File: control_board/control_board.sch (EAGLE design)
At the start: 37 parts, among them IC1 ATMEGA1284P-MU, J1 USB Female Type C Connector, Q1 220mA/50V/3.5Ω, SW1 SPST_TACT-KMR2, U1 915MHz, U3 MCP73833

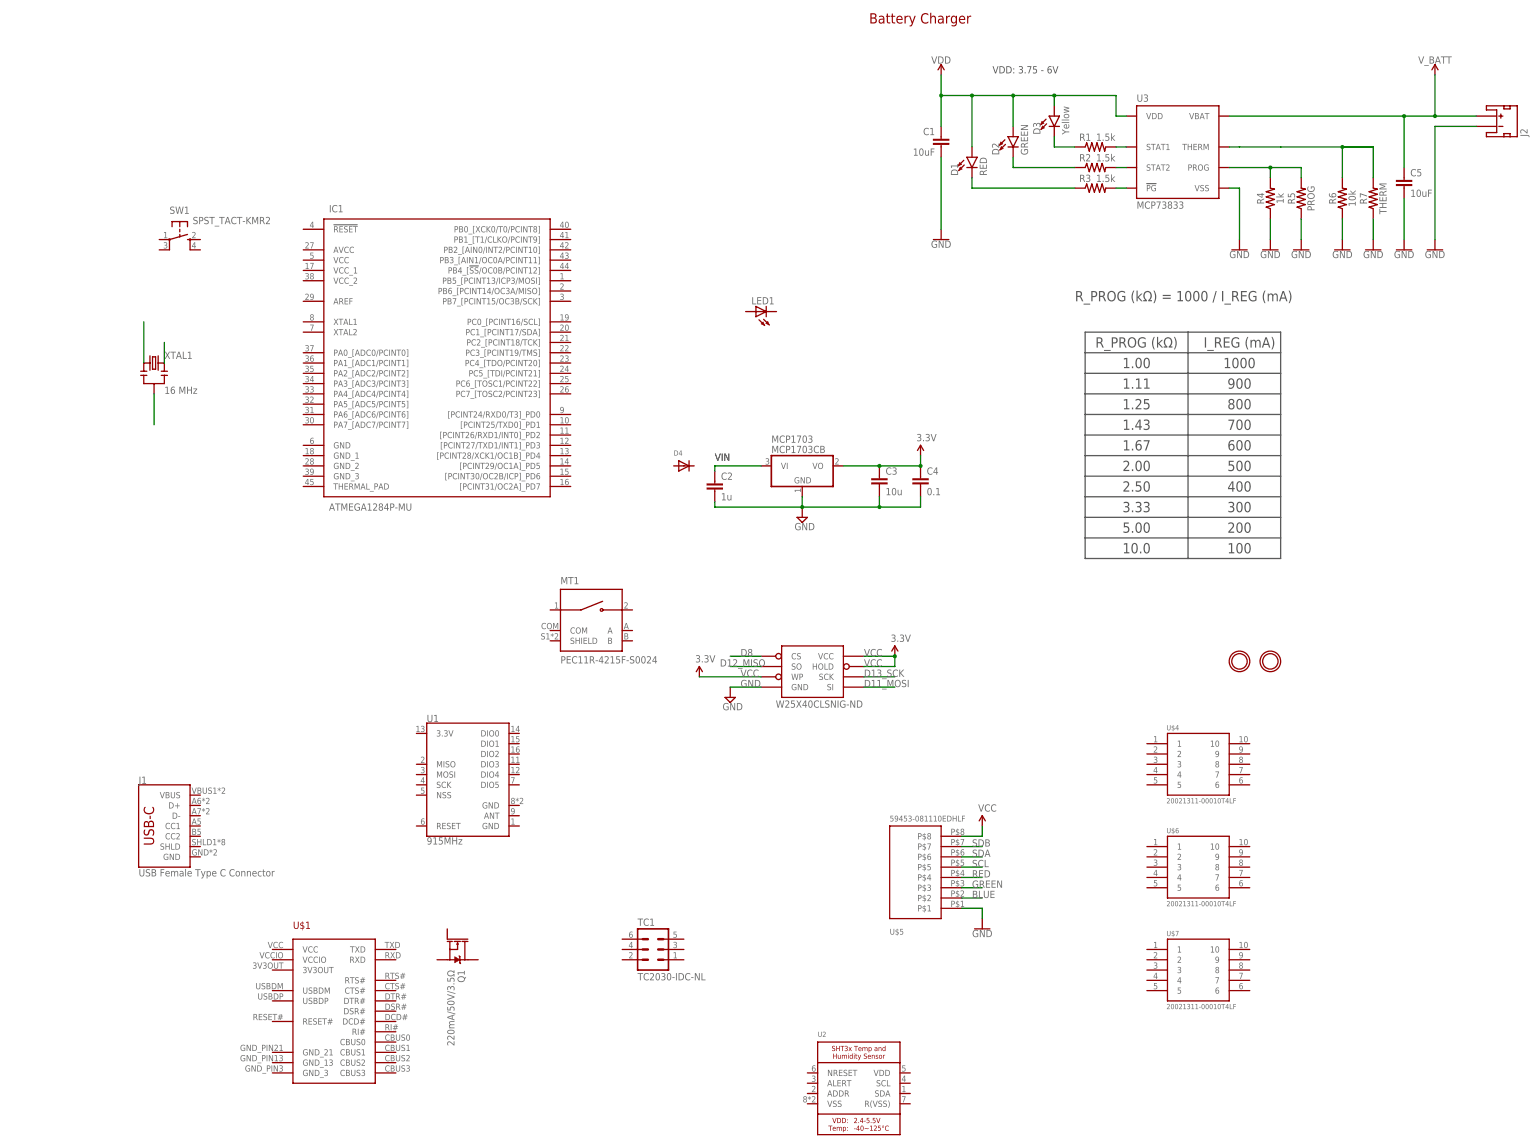
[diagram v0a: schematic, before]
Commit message: updated control board (unfinished)
- Schematic complete
- all components placed on board in roughly the approx. location
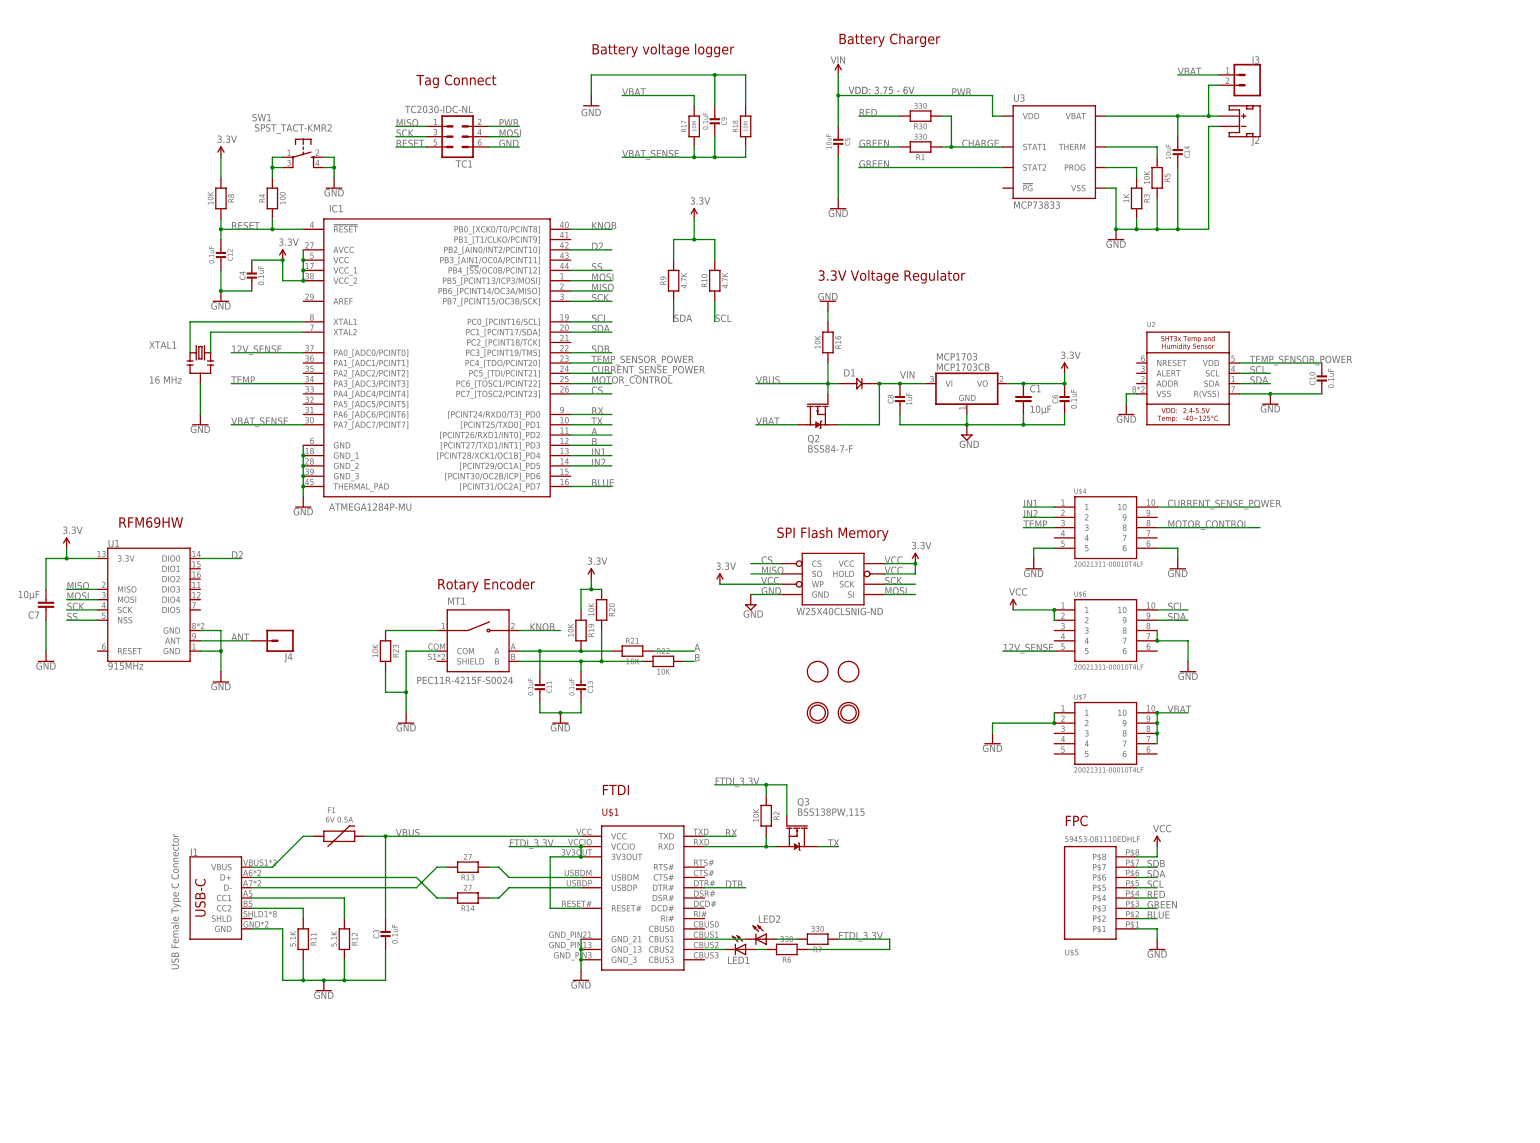
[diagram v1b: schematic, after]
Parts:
- removed C2: 1u, LowPowerLab:CAP0603-CAP
- removed D2: GREEN, SparkFun-LED:LED-GREEN0603
- removed D3: Yellow, SparkFun-LED:LED-YELLOW0603
- removed D4: (no value), adafruit:DIODESOD-123
- removed Q1: 220mA/50V/3.5Ω, SparkFun-DiscreteSemi:MOSFET-NCH-BSS138
- added C10, C11, C12, C13, C6, C9: 0.1uF, Adafruit Feather 32u4 Bluefruit LE:MICROBUILDER_CAP_CERAMIC_0402MP
- added C14: 10uF, Adafruit Feather 32u4 Bluefruit LE:MICROBUILDER_CAP_CERAMIC_0402MP
- added C7: 10µF, SparkFun-Capacitors:0.33UF/330NF-0805-50V-10%
- added C8: 1uF, Adafruit Feather 32u4 Bluefruit LE:MICROBUILDER_CAP_CERAMIC_0402MP
- added F1: 6V 0.5A, SparkFun-Fuses:PPTC_6V500MA
- added J3: (no value), SparkFun-Connectors:CONN_02
- added J4: (no value), SparkFun-Connectors:CONN_01
- added LED2: (no value), adafruit:LEDCHIPLED_0603
- added Q2: BSS84-7-F, MOSFETs:MOSFET-PCH-BSS84
- added Q3: BSS138PW,115, MOSFETs:MOSFET-NCH-BSS138PW,115
- added R10, R9: 4.7K, Adafruit Feather 32u4 Bluefruit LE:MICROBUILDER_RESISTOR_0402MP
- added R11, R12: 5.1K, Adafruit Feather 32u4 Bluefruit LE:MICROBUILDER_RESISTOR_0402MP
- added R13, R14: 27, Adafruit Feather 32u4 Bluefruit LE:MICROBUILDER_RESISTOR_0402MP
- added R16, R19, R20, R21, R22, R23, R8: 10K, Adafruit Feather 32u4 Bluefruit LE:MICROBUILDER_RESISTOR_0402MP
- added R17, R18: 10M, Adafruit Feather 32u4 Bluefruit LE:MICROBUILDER_RESISTOR_0402MP
- added R30: 330, Adafruit Feather 32u4 Bluefruit LE:MICROBUILDER_RESISTOR_0402MP
- added U$8, U$9: FIDUCIAL, adafruit:FIDUCIAL
- C1: value 10uF -> 10µF; device SparkFun-Capacitors:10UF-0603-6.3V-20% -> SparkFun-Capacitors:0.33UF/330NF-0805-50V-10%
- C3: value 10u -> 0.1uF; device LowPowerLab:CAP0805-CAP -> Adafruit Feather 32u4 Bluefruit LE:MICROBUILDER_CAP_CERAMIC_0402MP; MPN (none) -> GRM155R71C104KA88J
- C4: value 0.1 -> 0.1uF; device LowPowerLab:CAP0603-CAP -> Adafruit Feather 32u4 Bluefruit LE:MICROBUILDER_CAP_CERAMIC_0402MP; MPN (none) -> GRM155R71C104KA88J
- C5: device SparkFun-Capacitors:10UF-0603-6.3V-20% -> Adafruit Feather 32u4 Bluefruit LE:MICROBUILDER_CAP_CERAMIC_0402MP; MPN (none) -> GRM155R71C104KA88J
- D1: value RED -> (none); device SparkFun-LED:LED-RED0603 -> SCHOTTKY_0805:DIODE_SCHOTTKY0805-RES
- LED1: device adafruit:LEDCHIPLED_0805 -> adafruit:LEDCHIPLED_0603
- R1: value 1.5k -> 330; device SparkFun-Resistors:1.5KOHM-0603-1/10W-1% -> Adafruit Feather 32u4 Bluefruit LE:MICROBUILDER_RESISTOR_0402MP; MPN (none) -> RC0402FR-7W10KL
- R2: value 1.5k -> 10K; device SparkFun-Resistors:1.5KOHM-0603-1/10W-1% -> Adafruit Feather 32u4 Bluefruit LE:MICROBUILDER_RESISTOR_0402MP; MPN (none) -> RC0402FR-7W10KL
- R3: value 1.5k -> 1K; device SparkFun-Resistors:1.5KOHM-0603-1/10W-1% -> Adafruit Feather 32u4 Bluefruit LE:MICROBUILDER_RESISTOR_0402MP; MPN (none) -> RC0402FR-7W10KL
- R4: value 1k -> 100; device SparkFun-Resistors:1KOHM-0603-1/10W-1% -> Adafruit Feather 32u4 Bluefruit LE:MICROBUILDER_RESISTOR_0402MP; MPN (none) -> RC0402FR-7W10KL
- R5: value PROG -> 10K; device SparkFun-Resistors:RESISTORAXIAL-0.3 -> Adafruit Feather 32u4 Bluefruit LE:MICROBUILDER_RESISTOR_0402MP; MPN (none) -> RC0402FR-7W10KL
- R6: value 10k -> 330; device SparkFun-Resistors:10KOHM-0603-1/10W-1% -> Adafruit Feather 32u4 Bluefruit LE:MICROBUILDER_RESISTOR_0402MP; MPN (none) -> RC0402FR-7W10KL
- R7: value THERM -> 330; device SparkFun-Resistors:RESISTORAXIAL-0.3 -> Adafruit Feather 32u4 Bluefruit LE:MICROBUILDER_RESISTOR_0402MP; MPN (none) -> RC0402FR-7W10KL
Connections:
- removed net D11_MOSI: W25X40CLSNIG-ND.SI
- removed net D12_MISO: W25X40CLSNIG-ND.SO
- removed net D13_SCK: W25X40CLSNIG-ND.SCK
- removed net D8: W25X40CLSNIG-ND.CS
- removed net GND1: XTAL1.2
- removed net N$21: XTAL1.3
- removed net PG: R3.2, U3.!PG
- removed net STAT1: R1.2, U3.STAT1
- removed net STAT2: R2.2, U3.STAT2
- removed net VDD: C1.1, D1.A, D2.A, D3.A, U3.VDD
- removed net V_BATT: C5.1, J2.+, U3.VBAT
- new net 12V_SENSE: IC1.PA0_[ADC0/PCINT0], U$6.5
- new net A: C11.2, IC1.[PCINT26/RXD1/INT0]_PD2, MT1.A, R19.2, R21.1, R21.2
- new net ANT: J4.1, U1.ANT
- new net B: C13.2, IC1.[PCINT27/TXD1/INT1]_PD3, MT1.B, R20.2, R22.1, R22.2
- new net CHARGE: R1.1, R30.1, U3.STAT1
- new net CS: IC1.PC7_[TOSC2/PCINT23], W25X40CLSNIG-ND.CS
- new net CURRENT_SENSE_POWER: IC1.PC5_[TDI/PCINT21], U$4.10
- new net D2: IC1.PB2_[AIN0/INT2/PCINT10], U1.DIO0
- new net DTR: U$1.DTR#
- new net FTDI_3.3V: Q3.G, R2.1, R6.1, R7.1, U$1.3V3OUT, U$1.RESET#, U$1.VCCIO
- new net IN1: IC1.[PCINT28/XCK1/OC1B]_PD4, U$4.1
- new net IN2: IC1.[PCINT29/OC1A]_PD5, U$4.2
- new net KNOB: IC1.PB0_[XCK0/T0/PCINT8], MT1.2
- new net MISO: IC1.PB6_[PCINT14/OC3A/MISO], TC1.1, U1.MISO, W25X40CLSNIG-ND.SO
- new net MOSI: IC1.PB5_[PCINT13/ICP3/MOSI], TC1.4, U1.MOSI, W25X40CLSNIG-ND.SI
- new net MOTOR_CONTROL: IC1.PC6_[TOSC1/PCINT22], U$4.8
- new net N$10: F1.1, J1.VBUS
- new net N$11: MT1.1, R23.1
- new net N$12: R4.2, SW1.P, SW1.P1
- new net N$13: LED1.C, U$1.CBUS2
- new net N$14: Q3.S, R2.2, U$1.RXD
- new net N$15: LED1.A, R6.2
- new net N$17: LED2.A, R7.2
- new net N$18: LED2.C, U$1.CBUS1
- new net N$2: C14.2, J2.+, J3.2, U3.VBAT
- new net N$3: IC1.XTAL2, XTAL1.3
- new net N$7: J1.D-, R13.2
- new net N$8: R14.1, U$1.USBDP
- new net N$9: R13.1, U$1.USBDM
- new net PWR: C5.2, TC1.2, U3.VDD
- new net RESET: C12.2, IC1.!RESET, R4.1, R8.2, TC1.5
- new net RX: IC1.[PCINT24/RXD0/T3]_PD0, U$1.TXD
- new net SCK: IC1.PB7_[PCINT15/OC3B/SCK], TC1.3, U1.SCK, W25X40CLSNIG-ND.SCK
- new net SS: IC1.PB4_[!SS!/OC0B/PCINT12], U1.NSS
- new net TEMP: IC1.PA3_[ADC3/PCINT3], U$4.3
- new net TEMP_SENSOR_POWER: C10.1, IC1.PC4_[TDO/PCINT20], U2.VDD
- new net TX: IC1.[PCINT25/TXD0]_PD1, Q3.D
- new net VBAT: J3.1, Q2.D1, R17.2, U$7.10, U$7.7, U$7.8, U$7.9
- new net VBAT_SENSE: C9.1, IC1.PA7_[ADC7/PCINT7], R17.1, R18.1
- new net VBUS: C3.1, D1.1, F1.2, Q2.G1, R16.2, U$1.VCC
- net BLUE: now also IC1.[PCINT31/OC2A]_PD7
- net GND: now also C10.2, C11.1, C12.1, C13.1, C14.1, C5.1, C6.2, C7.1, C8.2, C9.2, IC1.GND, IC1.GND_1, IC1.GND_2, IC1.GND_3, IC1.THERMAL_PAD, J1.GND, MT1.COM, R11.2, R12.2, R16.1, R18.2, R23.2, R3.2, R5.2, SW1.S, SW1.S1, TC1.6, U$1.GND_13, U$1.GND_21, U$1.GND_3, U$4.5, U$4.6, U$6.7, U$6.8, U$7.1, U$7.2, U1.GND@1, U1.GND@2, U2.R(VSS), U2.VSS, XTAL1.2; no longer C2.2, C5.2, R4.1, R5.1, R6.1, R7.1
- net GREEN: now also R1.2, U3.STAT2
- net N$1: now also IC1.XTAL1
- net N$4: now also J1.CC2, R11.1; no longer D1.C, R3.1
- net N$5: now also J1.CC1, R12.1; no longer D2.C, R2.1
- net N$6: now also J1.D+, R14.2; no longer D3.C, R1.1
- net PROG: now also R3.1; no longer R4.2, R5.2
- net RED: now also R30.2
- net SCL: now also IC1.PC0_[PCINT16/SCL], R10.1, U$6.10, U2.SCL
- net SDA: now also IC1.PC1_[PCINT17/SDA], R9.1, U$6.9, U2.SDA
- net SDB: now also IC1.PC3_[PCINT19/TMS]
- net THERM: now also R5.1; no longer R6.2, R7.2
- net VCC: now also C1.1, C6.1, C7.2, IC1.AVCC, IC1.VCC, IC1.VCC_1, IC1.VCC_2, R10.2, R19.1, R20.1, R8.1, R9.2, U$6.1, U$6.2, U1.3.3V; no longer C3.1
- net VIN: now also C8.1, D1.2, Q2.S1; no longer C2.1
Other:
- note added: "3.3V Voltage Regulator"
- note added: "Battery voltage logger"
- note added: "FPC"
- note added: "FTDI"
- note added: "RFM69HW"
- note added: "Rotary Encoder"
- note added: "SPI Flash Memory"
- note added: "Tag Connect"
- note removed: "1.00"
- note removed: "1.11"
- note removed: "1.25"
- note removed: "1.43"
- note removed: "1.67"
- note removed: "10.0"
- note removed: "100"
- note removed: "1000"
- note removed: "2.00"
- note removed: "2.50"
- note removed: "200"
- note removed: "3.33"
- note removed: "300"
- note removed: "400"
- note removed: "5.00"
- note removed: "500"
- note removed: "600"
- note removed: "700"
- note removed: "800"
- note removed: "900"
- note removed: "I_REG (mA)"
- note removed: "R_PROG (kΩ)"
- note removed: "R_PROG (kΩ) = 1000 / I_REG (mA)"
- moved on the sheet: C1, C3, C4, C5, J1, J2, LED1, MCP1703, MT1, SW1, TC1, U$1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

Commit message: v0.1 - finished design
- Added gerbers, renders, dxf
- Updated dimensions
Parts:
- F1: value 6V 0.5A -> 10V 1.5A
- renumbered MCP1703 to U4, U$1 to U8, U$4 to J7, U$5 to U5, U$6 to J6, U$7 to J5, W25X40CLSNIG-ND to U7
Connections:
- net N$2 renamed VBAT_CHG
- removed net PWR: C5.2, TC1.2, U3.VDD
- new net CHANNEL_A: IC1.[PCINT26/RXD1/INT0]_PD2, R21.2
- new net CHANNEL_B: IC1.[PCINT27/TXD1/INT1]_PD3, R22.2
- net A: no longer IC1.[PCINT26/RXD1/INT0]_PD2, R21.2
- net B: no longer IC1.[PCINT27/TXD1/INT1]_PD3, R22.2
- net DTR: now also C12.1
- net GND: no longer C12.1
- net VBUS: now also C5.2, TC1.2, U3.VDD
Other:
- moved on the sheet: C10, F1, J2, J3, R16
